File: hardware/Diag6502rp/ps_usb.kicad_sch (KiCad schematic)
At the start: 15 parts, among them J5 USB4105-G-FA, U1 TLV74311P, U2 IP4234CZ6, U3 AP2112K-3.3

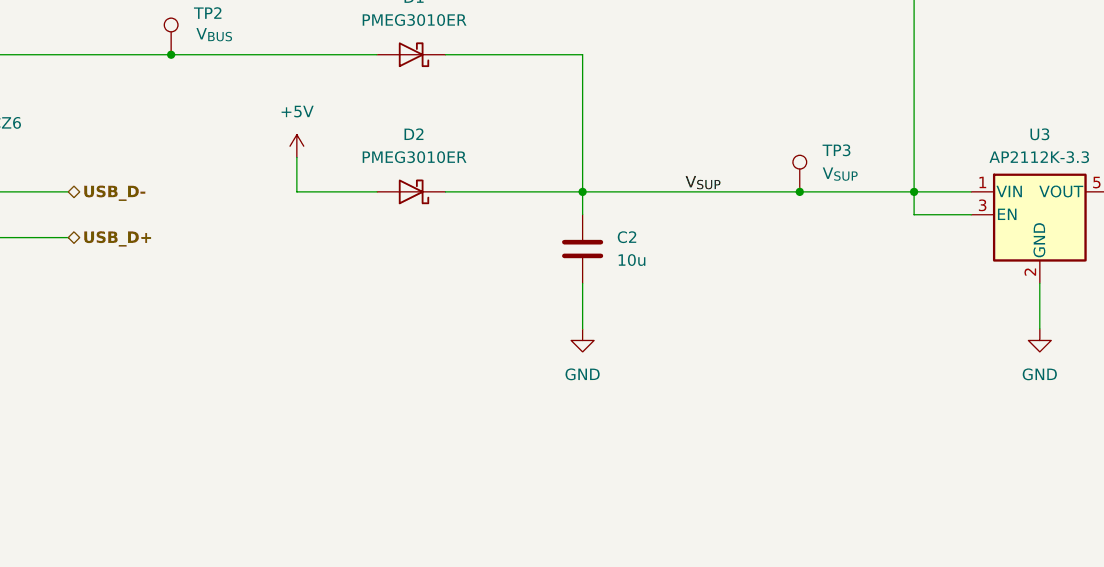
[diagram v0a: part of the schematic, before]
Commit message: Changed TSX0108e foorprint to TSSOP20 for easier routing.
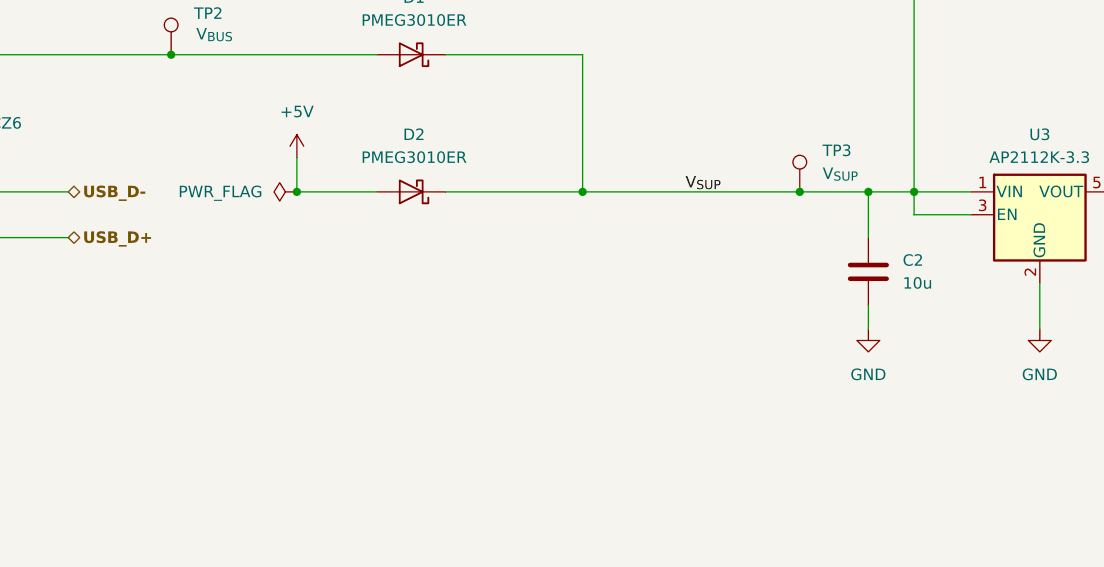
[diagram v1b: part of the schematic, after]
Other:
- moved on the sheet: C2
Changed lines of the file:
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@@
+	)
+	(junction
+		(at 179.07 69.85)
+		(diameter 0)
+		(color 0 0 0 0)
 	)
 	(junction
@@
 	)
 	(junction
+		(at 115.57 69.85)
+		(diameter 0)
+		(color 0 0 0 0)
+	)
+	(junction
 		(at 72.39 54.61)
 		(diameter 0)
@@
 	(wire
 		(pts
-			(xy 171.45 69.85) (xy 184.15 69.85)
+			(xy 171.45 69.85) (xy 179.07 69.85)
 		)
 		(stroke
@@
 	(wire
 		(pts
+			(xy 179.07 69.85) (xy 179.07 74.93)
+		)
+		(stroke
+			(width 0)
+			(type default)
+		)
+	)
+	(wire
+		(pts
 			(xy 205.74 34.29) (xy 217.17 34.29)
 		)
@@
 	(wire
 		(pts
+			(xy 179.07 82.55) (xy 179.07 85.09)
+		)
+		(stroke
+			(width 0)
+			(type default)
+		)
+	)
+	(wire
+		(pts
 			(xy 72.39 82.55) (xy 72.39 85.09)
 		)
@@
 	(wire
 		(pts
+			(xy 171.45 69.85) (xy 147.32 69.85)
+		)
+		(stroke
+			(width 0)
+			(type default)
+		)
+	)
+	(wire
+		(pts
 			(xy 115.57 69.85) (xy 124.46 69.85)
 		)
@@
 	(wire
 		(pts
+			(xy 179.07 69.85) (xy 184.15 69.85)
+		)
+		(stroke
+			(width 0)
+			(type default)
+		)
+	)
+	(wire
+		(pts
 			(xy 190.5 34.29) (xy 184.15 34.29)
 		)
@@
 	(wire
 		(pts
-			(xy 147.32 69.85) (xy 147.32 72.39)
-		)
-		(stroke
-			(width 0)
-			(type default)
-		)
-	)
-	(wire
-		(pts
 			(xy 48.26 72.39) (xy 48.26 74.93)
 		)
@@
 	(wire
 		(pts
-			(xy 147.32 69.85) (xy 171.45 69.85)
-		)
-		(stroke
-			(width 0)
-			(type default)
-		)
-	)
-	(wire
-		(pts
 			(xy 184.15 72.39) (xy 190.5 72.39)
 		)
@@
 		(pts
 			(xy 147.32 54.61) (xy 132.08 54.61)
-		)
-		(stroke
-			(width 0)
-			(type default)
-		)
-	)
-	(wire
-		(pts
-			(xy 147.32 80.01) (xy 147.32 85.09)
 		)
 		(stroke
@@
 	(symbol
 		(lib_id "Device:C")
-		(at 147.32 76.2 0)
+		(at 179.07 78.74 0)
 		(unit 1)
 		(exclude_from_sim no)
@@
 		(fields_autoplaced yes)
 		(property "Reference" "C2"
-			(at 151.13 74.9299 0)
+			(at 182.88 77.4699 0)
 			(effects
 				(font
@@
 		)
 		(property "Value" "10u"
-			(at 151.13 77.4699 0)
+			(at 182.88 80.0099 0)
 			(effects
 				(font
@@
 		)
 		(property "Footprint" "Capacitor_SMD:C_0603_1608Metric_Pad1.08x0.95mm_HandSolder"
-			(at 148.2852 80.01 0)
+			(at 180.0352 82.55 0)
 			(effects
 				(font
@@
 		)
 		(property "Datasheet" "~"
-			(at 147.32 76.2 0)
+			(at 179.07 78.74 0)
 			(effects
 				(font
@@
 		)
 		(property "Description" "Unpolarized capacitor"
-			(at 147.32 76.2 0)
+			(at 179.07 78.74 0)
 			(effects
 				(font
@@
 		)
 		(property "Feld9" ""
-			(at 147.32 76.2 0)
+			(at 179.07 78.74 0)
 			(effects
 				(font
@@
 		)
 		(property "Dielectric" "X7R"
-			(at 147.32 76.2 0)
+			(at 179.07 78.74 0)
 			(effects
 				(font
@@
 	(symbol
 		(lib_id "power:GND")
-		(at 147.32 85.09 0)
+		(at 179.07 85.09 0)
 		(unit 1)
 		(exclude_from_sim no)
@@
 		(fields_autoplaced yes)
 		(property "Reference" "#PWR09"
-			(at 147.32 91.44 0)
+			(at 179.07 91.44 0)
 			(effects
 				(font
@@
 		)
 		(property "Value" "GND"
-			(at 147.32 90.17 0)
+			(at 179.07 90.17 0)
 			(effects
 				(font
@@
 		)
 		(property "Footprint" ""
-			(at 147.32 85.09 0)
+			(at 179.07 85.09 0)
 			(effects
 				(font
@@
 		)
 		(property "Datasheet" ""
-			(at 147.32 85.09 0)
+			(at 179.07 85.09 0)
 			(effects
 				(font
@@
 		)
 		(property "Description" "Power symbol creates a global label with name \"GND\" , ground"
-			(at 147.32 85.09 0)
+			(at 179.07 85.09 0)
 			(effects
 				(font
@@
 					(unit 1)
 				)
+			)
+		)
+	)
+	(symbol
+		(lib_id "power:PWR_FLAG")
+		(at 115.57 69.85 90)
+		(unit 1)
+		(exclude_from_sim no)
+		(in_bom yes)
+		(on_board yes)
+		(dnp no)
+		(fields_autoplaced yes)
+		(property "Reference" "#FLG08"
+			(at 113.665 69.85 0)
+			(effects
+				(font
+					(size 1.27 1.27)
+				)
+				(hide yes)
+			)
+		)
+		(property "Value" "PWR_FLAG"
+			(at 111.76 69.8499 90)
+			(effects
+				(font
+					(size 1.27 1.27)
+				)
+				(justify left)
+			)
+		)
+		(property "Footprint" ""
+			(at 115.57 69.85 0)
+			(effects
+				(font
+					(size 1.27 1.27)
+				)
+				(hide yes)
+			)
+		)
+		(property "Datasheet" "~"
+			(at 115.57 69.85 0)
+			(effects
+				(font
+					(size 1.27 1.27)
+				)
+				(hide yes)
+			)
+		)
+		(property "Description" "Special symbol for telling ERC where power comes from"
+			(at 115.57 69.85 0)
+			(effects
+				(font
+					(size 1.27 1.27)
+				)
+				(hide yes)
+			)
+		)
+		(pin "1"
+		)
+		(instances
+			(project ""
+				(path "/2439caa5-1b7d-40de-b309-64357b0b1cd3/5ebef23f-13b0-4832-80ab-6dd0d052fbcf"
+					(reference "#FLG08")
+					(unit 1)
+				)

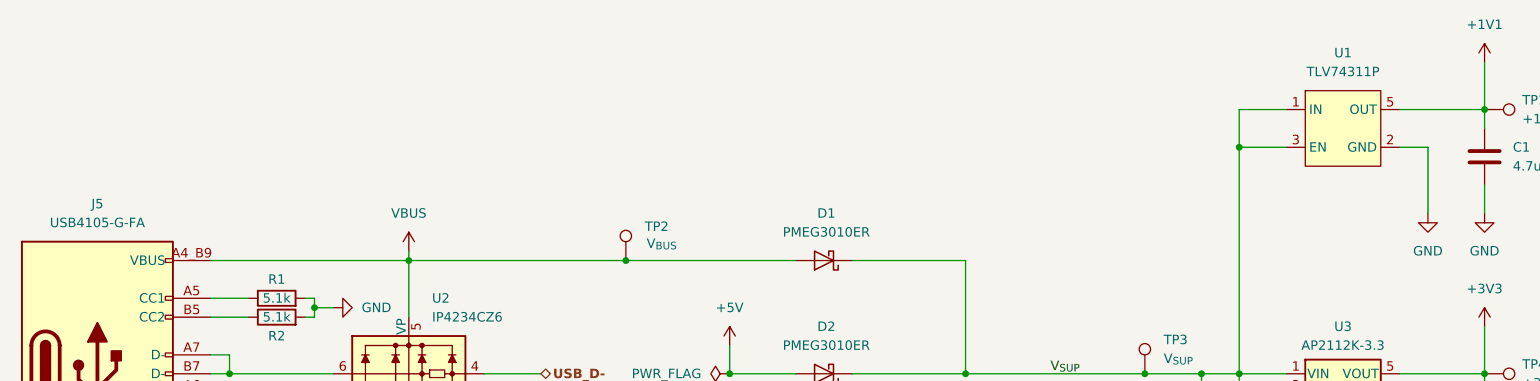
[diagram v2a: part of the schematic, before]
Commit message: Cleanup, Fiduciaries, component spacing
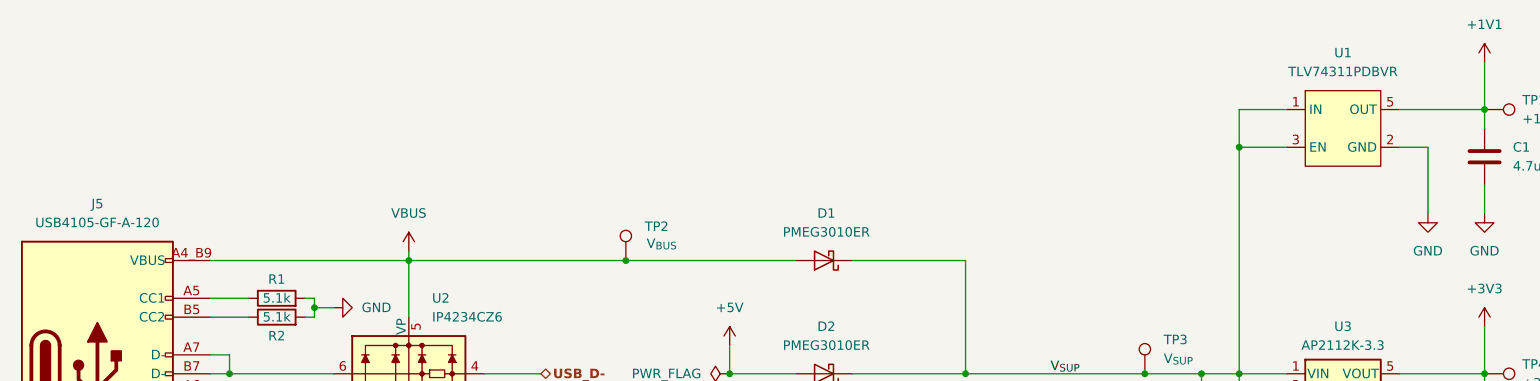
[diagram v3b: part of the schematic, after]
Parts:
- C1, C3: footprint Capacitor_SMD:C_0402_1005Metric_Pad0.74x0.62mm_HandSolder -> Capacitor_SMD:C_0402_1005Metric; LCSC Part # (none) -> C23733
- C2: footprint Capacitor_SMD:C_0603_1608Metric_Pad1.08x0.95mm_HandSolder -> Capacitor_SMD:C_0603_1608Metric; LCSC Part # (none) -> C19702
- D1, D2: LCSC Part # (none) -> C456106
- J5: value USB4105-G-FA -> USB4105-GF-A-120; LCSC Part # (none) -> C963370; Mouser Part # (none) -> 640-USB4105-GF-A-120
- R1, R2: footprint Resistor_SMD:R_0402_1005Metric_Pad0.72x0.64mm_HandSolder -> Resistor_SMD:R_0402_1005Metric; LCSC Part # (none) -> C25905
- TP1, TP2, TP3, TP4: now left out of the parts list
- U1: value TLV74311P -> TLV74311PDBVR; LCSC Part # (none) -> C485147
- U2: LCSC Part # (none) -> C455086
- U3: LCSC Part # (none) -> C51118

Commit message: preparing for assembly
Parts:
- J5: value USB4105-GF-A-120 -> GT-USB-7010AN
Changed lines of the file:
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@@
 			)
 		)
-		(property "Value" "USB4105-GF-A-120"
+		(property "Value" "GT-USB-7010AN"
 			(at 30.48 49.53 0)
 			(effects

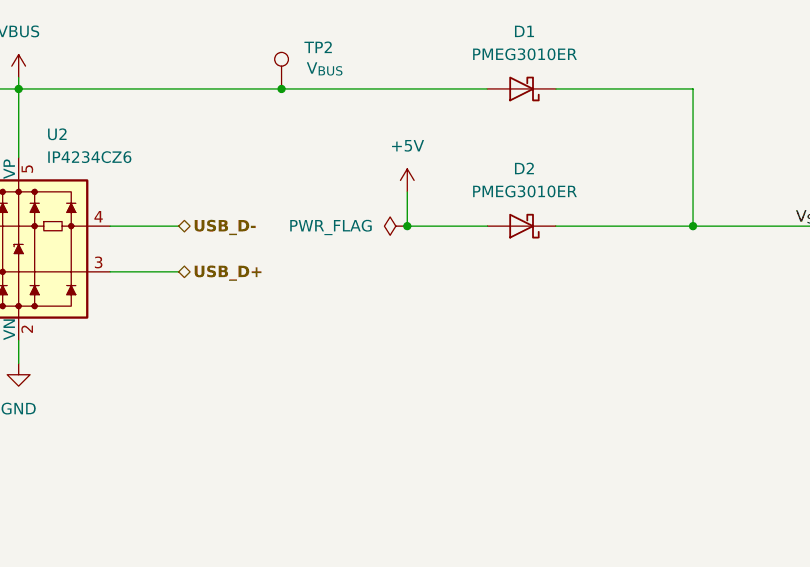
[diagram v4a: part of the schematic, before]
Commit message: Added transfer and stitching vias.
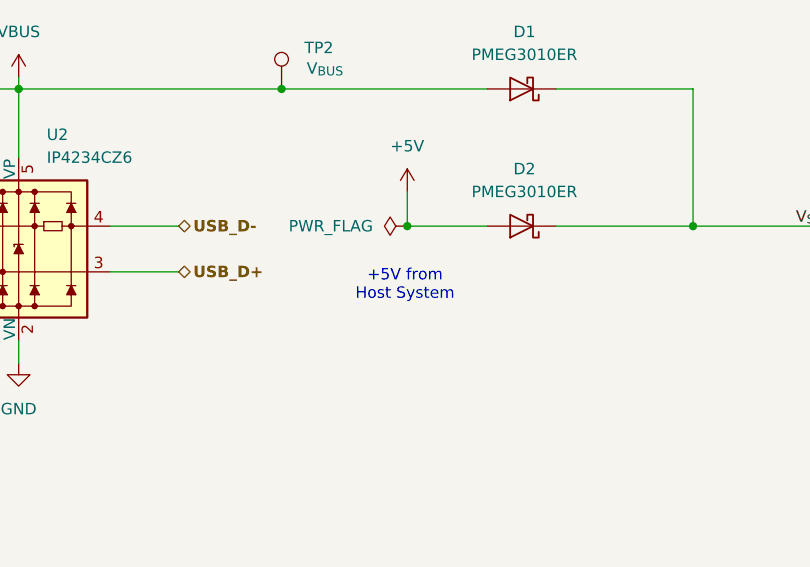
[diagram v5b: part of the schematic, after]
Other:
- note added: "+5V from Host System"
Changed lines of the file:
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@@
 	(generator_version "9.0")
 	(paper "A4")
+	(text "+5V from \nHost System"
+		(exclude_from_sim no)
+		(at 115.316 76.454 0)
+		(effects
+			(font
+				(size 1.27 1.27)
+			)
+		)
+	)
 	(junction
 		(at 48.26 74.93)

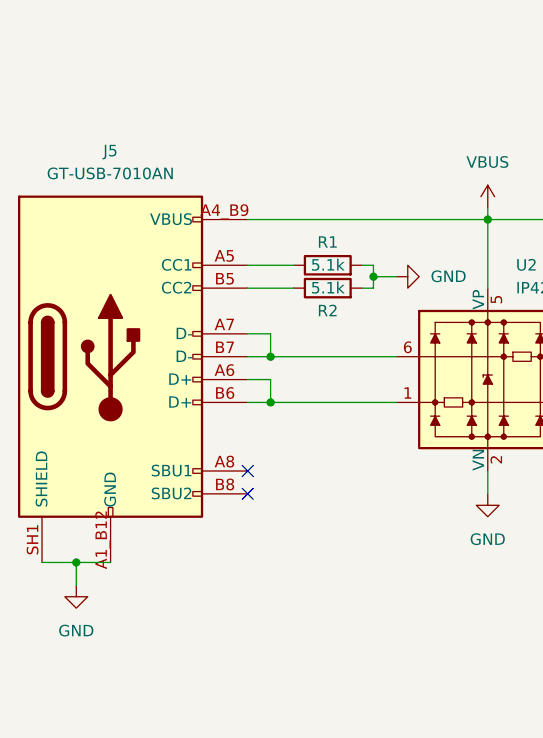
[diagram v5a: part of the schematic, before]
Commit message: More via separation and transfer vias
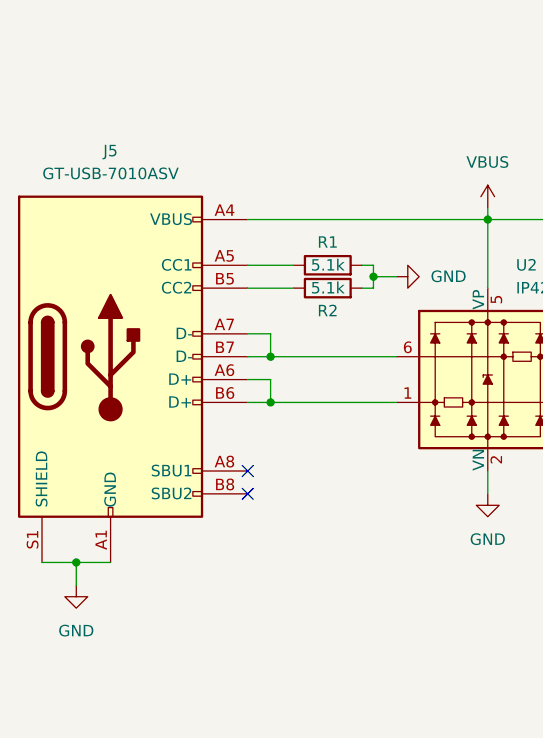
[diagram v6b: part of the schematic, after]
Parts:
- removed J5: GT-USB-7010AN, footprints:GCT_USB4105-GF-A, symbol symbol_library:USB4105-GF-A
- added J5: GT-USB-7010ASV, Connector_USB:USB_C_Receptacle_G-Switch_GT-USB-7010ASV, symbol Connector:USB_C_Receptacle_USB2.0_16P
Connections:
- net GND: now also J5.A1 (GND), J5.A12 (GND), J5.B1 (GND), J5.B12 (GND), J5.S1 (SHIELD)
- net VBUS: now also J5.A4 (VBUS), J5.A9 (VBUS), J5.B4 (VBUS), J5.B9 (VBUS)
- net at R1.1: now also J5.A5 (CC1)
- net at U2.1: now also J5.A6 (D+), J5.B6 (D+)
- net at U2.6: now also J5.A7 (D-), J5.B7 (D-)
- net at R2.1: now also J5.B5 (CC2)
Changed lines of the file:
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@@
+	)
+	(symbol
+		(lib_id "Connector:USB_C_Receptacle_USB2.0_16P")
+		(at 30.48 69.85 0)
+		(unit 1)
+		(exclude_from_sim no)
+		(in_bom yes)
+		(on_board yes)
+		(dnp no)
+		(fields_autoplaced yes)
+		(property "Reference" "J5"
+			(at 30.48 46.99 0)
+			(effects
+				(font
+					(size 1.27 1.27)
+				)
+			)
+		)
+		(property "Value" "GT-USB-7010ASV"
+			(at 30.48 49.53 0)
+			(effects
+				(font
+					(size 1.27 1.27)
+				)
+			)
+		)
+		(property "Footprint" "Connector_USB:USB_C_Receptacle_G-Switch_GT-USB-7010ASV"
+			(at 34.29 69.85 0)
+			(effects
+				(font
+					(size 1.27 1.27)
+				)
+				(hide yes)
+			)
+		)
+		(property "Datasheet" "https://www.usb.org/sites/default/files/documents/usb_type-c.zip"
+			(at 34.29 69.85 0)
+			(effects
+				(font
+					(size 1.27 1.27)
+				)
+				(hide yes)
+			)
+		)
+		(property "Description" "USB 2.0-only 16P Type-C Receptacle connector"
+			(at 30.48 69.85 0)
+			(effects
+				(font
+					(size 1.27 1.27)
+				)
+				(hide yes)
+			)
+		)
+		(pin "B12"
+		)
+		(pin "A9"
+		)
+		(pin "A5"
+		)
+		(pin "A7"
+		)
+		(pin "A6"
+		)
+		(pin "B5"
+		)
+		(pin "A1"
+		)
+		(pin "B9"
+		)
+		(pin "A8"
+		)
+		(pin "B8"
+		)
+		(pin "B1"
+		)
+		(pin "B4"
+		)
+		(pin "S1"
+		)
+		(pin "A12"
+		)
+		(pin "A4"
+		)
+		(pin "B7"
+		)
+		(pin "B6"
+		)
+		(instances
+			(project ""
+				(path "/2439caa5-1b7d-40de-b309-64357b0b1cd3/5ebef23f-13b0-4832-80ab-6dd0d052fbcf"
+					(reference "J5")
+					(unit 1)
+				)
+			)
+		)
 	)
 	(symbol
@@
 					(unit 1)
 				)
-			)
-		)
-	)
-	(symbol
-		(lib_id "symbol_library:USB4105-GF-A")
-		(at 30.48 69.85 0)
-		(unit 1)
-		(exclude_from_sim yes)
-		(in_bom yes)
-		(on_board yes)
-		(dnp no)
-		(fields_autoplaced yes)
-		(property "Reference" "J5"
-			(at 30.48 46.99 0)
-			(effects
-				(font
-					(size 1.27 1.27)
-				)
-			)
-		)
-		(property "Value" "GT-USB-7010AN"
-			(at 30.48 49.53 0)
-			(effects
-				(font
-					(size 1.27 1.27)
-				)
-			)
-		)
-		(property "Footprint" "footprints:GCT_USB4105-GF-A"
-			(at 34.29 69.85 0)
-			(effects
-				(font
-					(size 1.27 1.27)
-				)
-				(hide yes)
-			)
-		)
-		(property "Datasheet" "https://www.usb.org/sites/default/files/documents/usb_type-c.zip"
-			(at 34.29 69.85 0)
-			(effects
-				(font
-					(size 1.27 1.27)
-				)
-				(hide yes)
-			)
-		)
-		(property "Description" "USB 2.0-only 16P Type-C Receptacle connector"
-			(at 30.48 69.85 0)
-			(effects
-				(font
-					(size 1.27 1.27)
-				)
-				(hide yes)
-			)
-		)
-		(property "LCSC Part #" "C963370 "
-			(at 30.48 69.85 0)
-			(effects
-				(font
-					(size 1.27 1.27)
-				)
-				(hide yes)
-			)
-		)
-		(property "Mouser Part #" "640-USB4105-GF-A-120"
-			(at 30.48 69.85 0)
-			(effects
-				(font
-					(size 1.27 1.27)
-				)
-				(hide yes)
-			)
-		)
-		(property "LCSC Name" ""
-			(at 30.48 69.85 0)
-			(effects
-				(font
-					(size 1.27 1.27)
-				)
-				(hide yes)
-			)
-		)
-		(pin "SH1"
-		)
-		(pin "SH3"
-		)
-		(pin "SH4"
-		)
-		(pin "A1_B12"
-		)
-		(pin "B1_A12"
-		)
-		(pin "SH2"
-		)
-		(pin "B6"
-		)
-		(pin "B7"
-		)
-		(pin "B5"
-		)
-		(pin "A8"
-		)
-		(pin "A6"
-		)
-		(pin "A4_B9"
-		)
-		(pin "A5"
-		)
-		(pin "A7"
-		)
-		(pin "B4_A9"
-		)
-		(pin "B8"
-		)
-		(instances
-			(project ""
-				(path "/2439caa5-1b7d-40de-b309-64357b0b1cd3/5ebef23f-13b0-4832-80ab-6dd0d052fbcf"
-					(reference "J5")
-					(unit 1)
-				)
